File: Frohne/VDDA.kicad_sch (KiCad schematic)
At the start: 29 parts, among them J5 Conn_01x02, Q1 AO3401A, U6 L78M05ABDT-TR

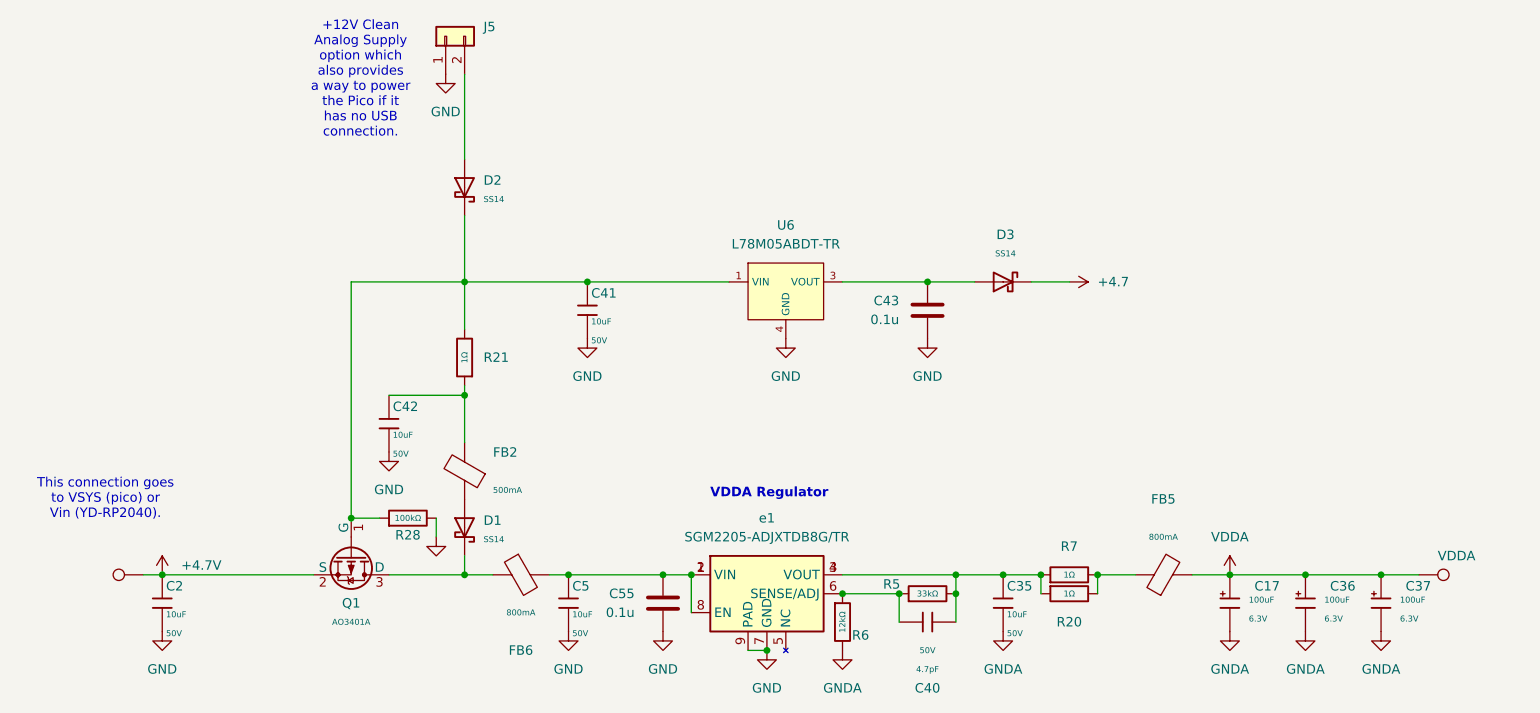
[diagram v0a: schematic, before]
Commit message: Fixed a few schematic errors.
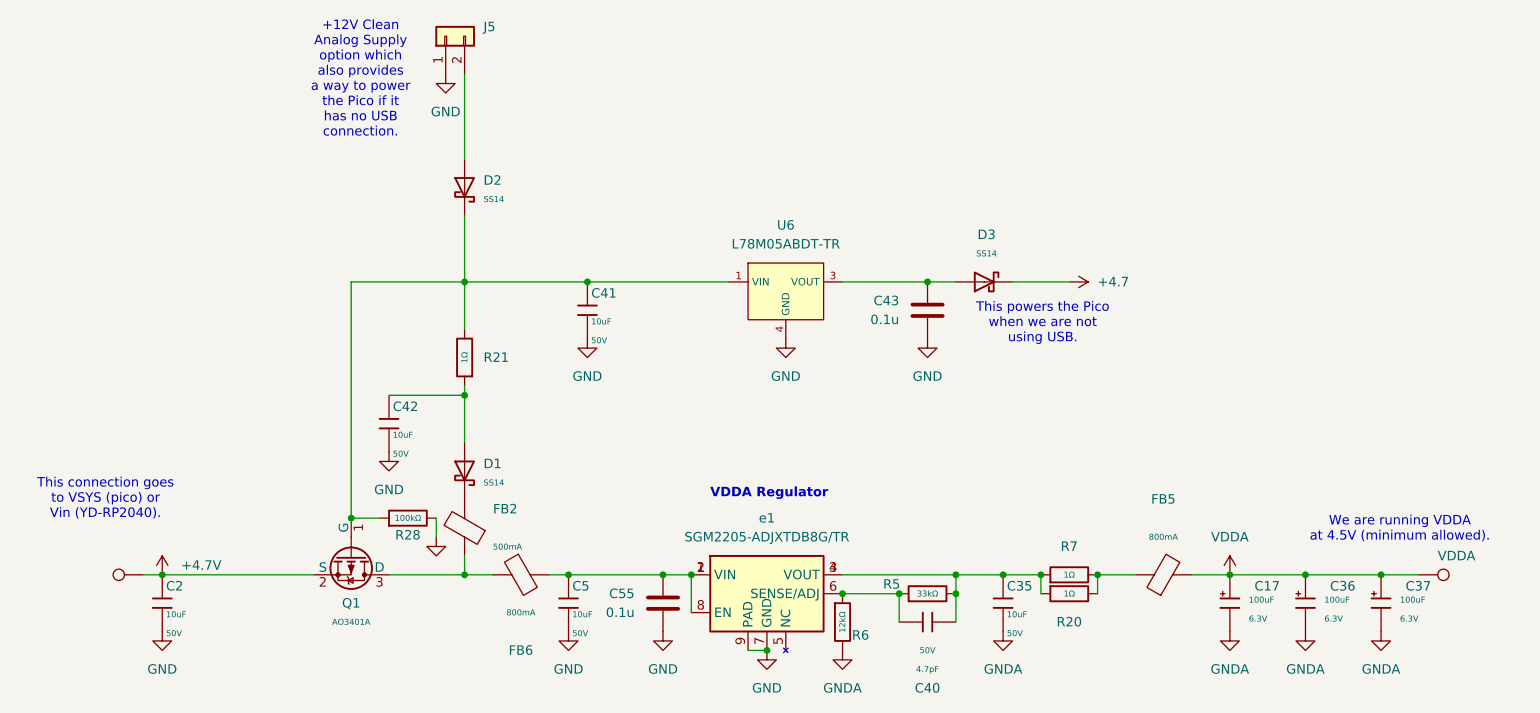
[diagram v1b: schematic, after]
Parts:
- TP25, TP26: footprint TestPoint:TestPoint_THTPad_D1.0mm_Drill0.5mm -> TestPoint:TestPoint_THTPad_D1.5mm_Drill0.7mm
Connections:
- net at C42.1, R21.1: now also D1.2; no longer FB2.2
- net at FB6.1, Q1.3 (D): now also FB2.1; no longer D1.1
- new net: D1.1, FB2.2
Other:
- note added: "This powers the Pico when we are not using USB."
- note added: "We are running VDDA at 4.5V (minimum allowed)."
- moved on the sheet: D1, D3, FB2
